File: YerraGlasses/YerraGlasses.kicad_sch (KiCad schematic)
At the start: 0 parts

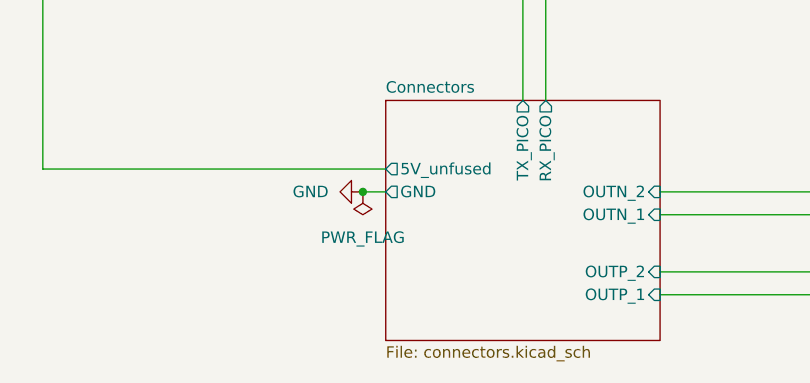
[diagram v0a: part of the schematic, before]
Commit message: added power connector, updated cad
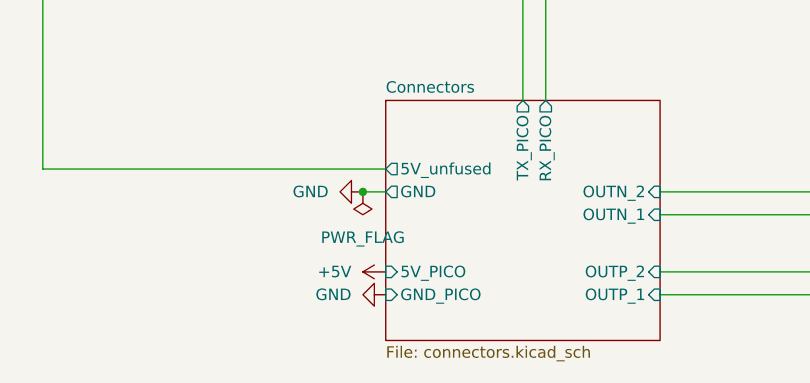
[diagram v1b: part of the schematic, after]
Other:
- sheet Connectors ports: added 5V_PICO, GND_PICO; removed none
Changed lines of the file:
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@@
+	)
+	(symbol
+		(lib_id "power:+5V")
+		(at 83.82 82.55 90)
+		(unit 1)
+		(exclude_from_sim no)
+		(in_bom yes)
+		(on_board yes)
+		(dnp no)
+		(fields_autoplaced yes)
+		(property "Reference" "#PWR014"
+			(at 87.63 82.55 0)
+			(effects
+				(font
+					(size 1.27 1.27)
+				)
+				(hide yes)
+			)
+		)
+		(property "Value" "+5V"
+			(at 80.01 82.5499 90)
+			(effects
+				(font
+					(size 1.27 1.27)
+				)
+				(justify left)
+			)
+		)
+		(property "Footprint" ""
+			(at 83.82 82.55 0)
+			(effects
+				(font
+					(size 1.27 1.27)
+				)
+				(hide yes)
+			)
+		)
+		(property "Datasheet" ""
+			(at 83.82 82.55 0)
+			(effects
+				(font
+					(size 1.27 1.27)
+				)
+				(hide yes)
+			)
+		)
+		(property "Description" "Power symbol creates a global label with name \"+5V\""
+			(at 83.82 82.55 0)
+			(effects
+				(font
+					(size 1.27 1.27)
+				)
+				(hide yes)
+			)
+		)
+		(pin "1"
+		)
+		(instances
+			(project ""
+				(path "/565dd4cd-3458-4e26-8cb8-cc6b370af252"
+					(reference "#PWR014")
+					(unit 1)
+				)
+			)
+		)
+	)
+	(symbol
+		(lib_id "power:GND")
+		(at 83.82 85.09 270)
+		(unit 1)
+		(exclude_from_sim no)
+		(in_bom yes)
+		(on_board yes)
+		(dnp no)
+		(fields_autoplaced yes)
+		(property "Reference" "#PWR015"
+			(at 77.47 85.09 0)
+			(effects
+				(font
+					(size 1.27 1.27)
+				)
+				(hide yes)
+			)
+		)
+		(property "Value" "GND"
+			(at 80.01 85.0899 90)
+			(effects
+				(font
+					(size 1.27 1.27)
+				)
+				(justify right)
+			)
+		)
+		(property "Footprint" ""
+			(at 83.82 85.09 0)
+			(effects
+				(font
+					(size 1.27 1.27)
+				)
+				(hide yes)
+			)
+		)
+		(property "Datasheet" ""
+			(at 83.82 85.09 0)
+			(effects
+				(font
+					(size 1.27 1.27)
+				)
+				(hide yes)
+			)
+		)
+		(property "Description" "Power symbol creates a global label with name \"GND\" , ground"
+			(at 83.82 85.09 0)
+			(effects
+				(font
+					(size 1.27 1.27)
+				)
+				(hide yes)
+			)
+		)
+		(pin "1"
+		)
+		(instances
+			(project ""
+				(path "/565dd4cd-3458-4e26-8cb8-cc6b370af252"
+					(reference "#PWR015")
+					(unit 1)
+				)
+			)
+		)
 	)
 	(symbol
@@
 			)
 		)
+		(pin "5V_PICO" input
+			(at 83.82 82.55 180)
+			(effects
+				(font
+					(size 1.27 1.27)
+				)
+				(justify left)
+			)
+		)
+		(pin "GND_PICO" input
+			(at 83.82 85.09 180)
+			(effects
+				(font
+					(size 1.27 1.27)
+				)
+				(justify left)
+			)
+		)

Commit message: cad completion prototype
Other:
- sheet Connectors ports: added 9V_unfused; removed 5V_unfused
- sheet Power ports: added 9V_unfused; removed 5V_unfused
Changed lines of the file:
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@@
 			)
 		)
-		(pin "5V_unfused" input
+		(pin "9V_unfused" input
 			(at 45.72 46.99 270)
 			(effects
@@
 			)
 		)
-		(pin "5V_unfused" output
+		(pin "9V_unfused" output
 			(at 83.82 71.12 180)
 			(effects

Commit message: updated pcb order, cad
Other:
- sheet Power ports: added USB_5V; removed USB_+5V
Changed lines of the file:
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@@
 			)
 		)
-		(pin "USB_+5V" input
+		(pin "USB_5V" input
 			(at 60.96 34.29 0)
 			(effects
